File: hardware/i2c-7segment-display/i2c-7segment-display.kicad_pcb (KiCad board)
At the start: 2 copper layers, 58.2 x 29 mm, 16 parts, among them J1 Conn_01x04

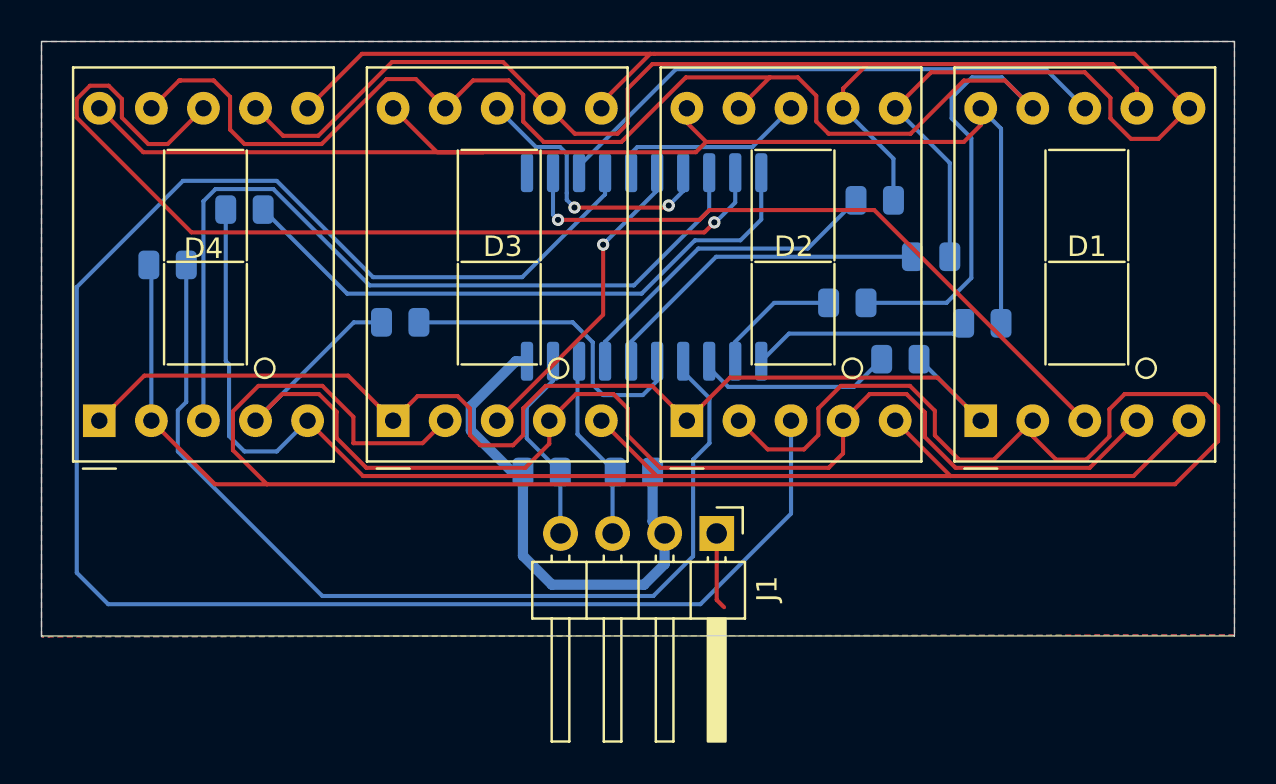
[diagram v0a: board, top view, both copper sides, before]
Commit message: fixed pcb errors
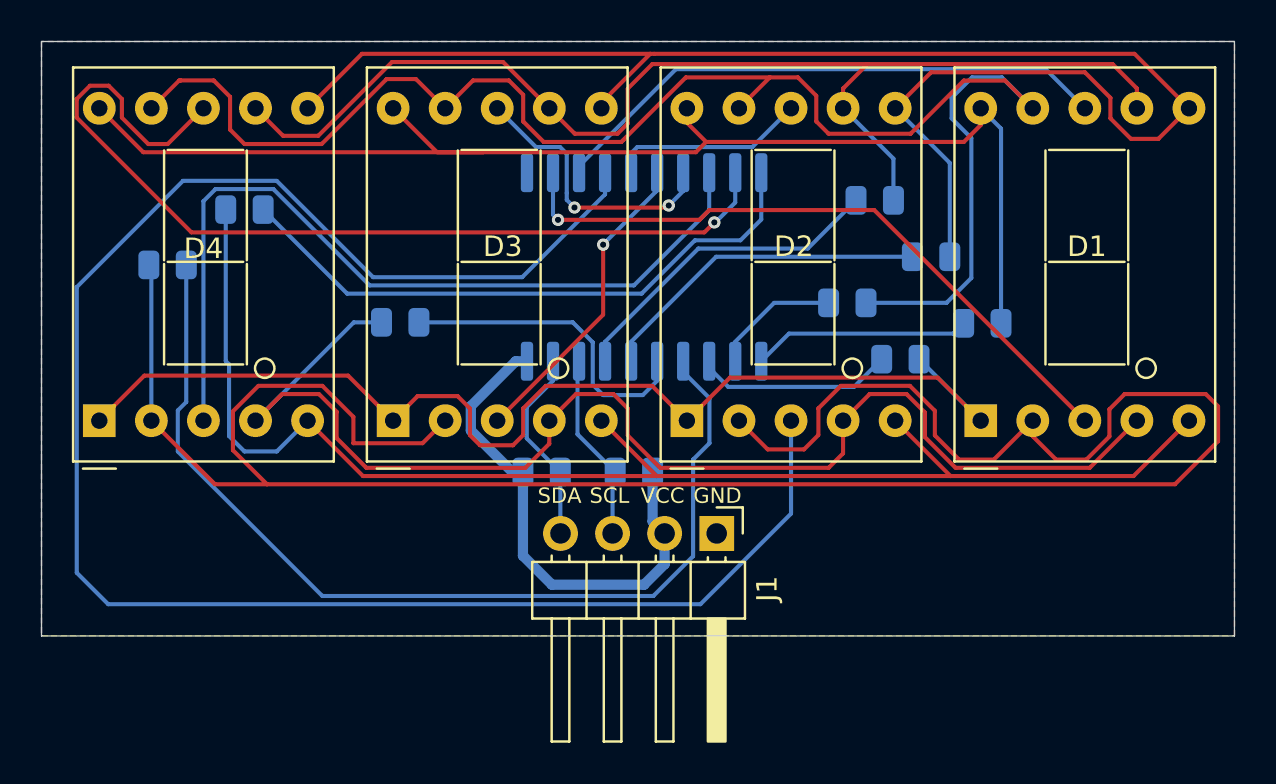
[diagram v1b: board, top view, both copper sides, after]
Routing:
- net GND: track 3.75 -> 0.00 mm
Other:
- board text added: "GND"
- board text added: "SCL"
- board text added: "SDA"
- board text added: "VCC"
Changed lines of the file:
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@@
 		(tenting front back)
 		(pcbplotparams
-			(layerselection 0x00000000_00000000_55555555_5755f5ff)
+			(layerselection 0x00000000_00000000_55555555_ff55f5ff)
 			(plot_on_all_layers_selection 0x00000000_00000000_00000000_00000000)
 			(disableapertmacros no)
@@
 			(outputformat 1)
 			(mirror no)
-			(drillshape 1)
+			(drillshape 0)
 			(scaleselection 1)
-			(outputdirectory "")
+			(outputdirectory "../gerber/")
 		)
 	)
@@
 		(layer "Edge.Cuts")
 	)
+	(gr_text "GND"
+		(at 164.4 115.6 0)
+		(layer "F.SilkS")
+		(effects
+			(font
+				(size 0.75 0.75)
+				(thickness 0.1)
+			)
+			(justify left bottom)
+		)
+	)
+	(gr_text "VCC"
+		(at 161.830953 115.6 0)
+		(layer "F.SilkS")
+		(effects
+			(font
+				(size 0.75 0.75)
+				(thickness 0.1)
+			)
+			(justify left bottom)
+		)
+	)
+	(gr_text "SCL"
+		(at 159.333333 115.6 0)
+		(layer "F.SilkS")
+		(effects
+			(font
+				(size 0.75 0.75)
+				(thickness 0.1)
+			)
+			(justify left bottom)
+		)
+	)
+	(gr_text "SDA"
+		(at 156.8 115.6 0)
+		(layer "F.SilkS")
+		(effects
+			(font
+				(size 0.75 0.75)
+				(thickness 0.1)
+			)
+			(justify left bottom)
+		)
+	)
 	(segment
 		(start 172.3375 100.75)
@@
 	)
 	(segment
-		(start 165.54 120.24)
-		(end 165.9 120.6)
-		(width 0.2)
-		(layer "F.Cu")
-		(net 19)
-	)
-	(segment
-		(start 165.54 117)
-		(end 165.54 120.24)
-		(width 0.2)
-		(layer "F.Cu")
-		(net 19)
-	)
-	(segment
 		(start 160.46 117)
 		(end 160.46 114.1275)
@@
 		(net 19)
 		(net_name "GND")
-		(layers "F.Cu" "B.Cu")
+		(layer "F.Cu")
+		(hatch edge 0.5)
+		(connect_pads yes
+			(clearance 0.2)
+		)
+		(min_thickness 0.2)
+		(filled_areas_thickness no)
+		(fill yes
+			(thermal_gap 0.5)
+			(thermal_bridge_width 0.5)
+		)
+		(polygon
+			(pts
+				(xy 132.6 93) (xy 132.6 122) (xy 190.8 122) (xy 190.8 93)
+			)
+		)
+	)
+	(zone
+		(net 19)
+		(net_name "GND")
+		(layer "B.Cu")
 		(hatch edge 0.5)
-		(connect_pads
-			(clearance 0.3)
+		(priority 1)
+		(connect_pads yes
+			(clearance 0.2)
 		)
 		(min_thickness 0.2)
@@
 			(thermal_gap 0.5)
 			(thermal_bridge_width 0.5)
-			(island_removal_mode 2)
-			(island_area_min 25)
 		)
 		(polygon
 			(pts
-				(xy 132.6 93) (xy 190.8 93) (xy 190.8 121.947591) (xy 132.6 122.047936)
+				(xy 190.8 122) (xy 190.8 93) (xy 132.6 93) (xy 132.6 122)
 			)
 		)
